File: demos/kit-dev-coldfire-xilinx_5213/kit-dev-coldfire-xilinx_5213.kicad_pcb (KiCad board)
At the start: 4 copper layers, 162 parts, among them J1 JACK_2P, P1 CONN_6, P3 CONN_2X2, P4 CONN_20X2, Q1 3906, SW1 SW_PUSH, SW2 SW_PUSH, U1 MCF5213-LQFP100, U2 74AHC1G14, U3 MAX202, U4 74HC125, U5 MAX202, U7 PCA82C251, U8 MAX202, U9 XCR3256-TQ144, Y1 8MHz

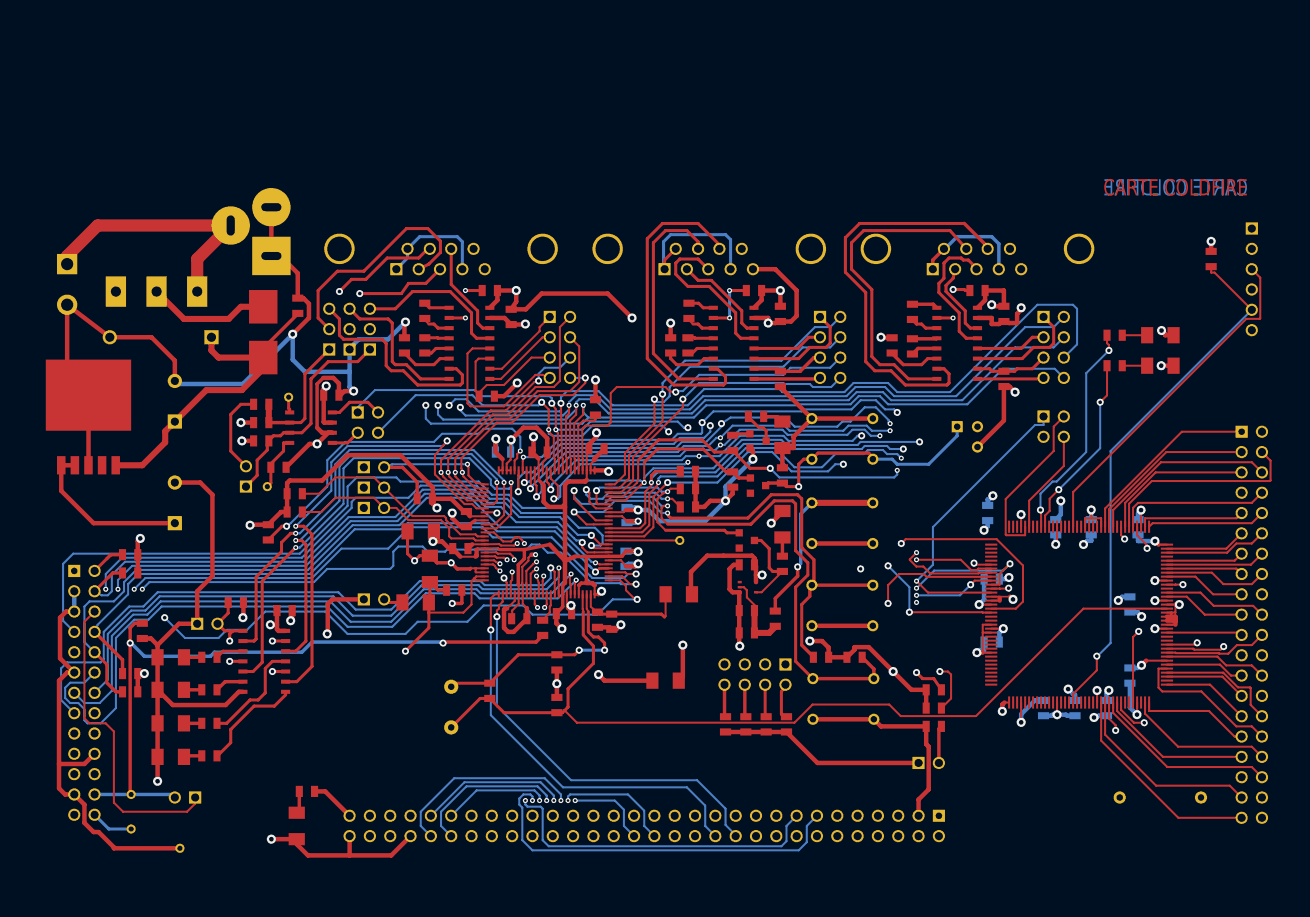
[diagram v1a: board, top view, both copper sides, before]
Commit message: Update demo files. A minor code cleaning.
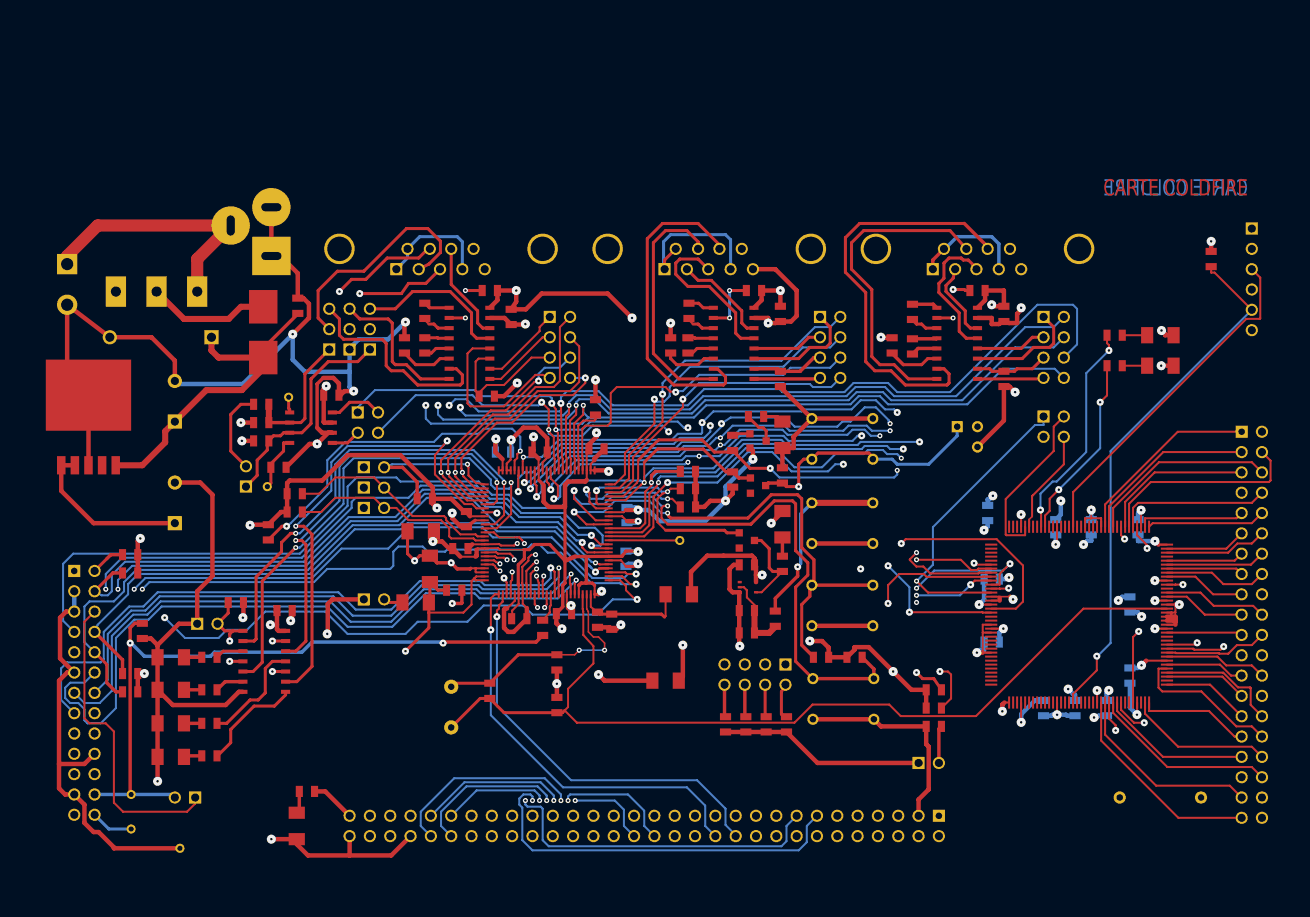
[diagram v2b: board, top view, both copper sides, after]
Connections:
- net +3.3V renamed VCC
- net /CANTX renamed /inout_user/CANTX
- net /DSPI_DOUT renamed /inout_user/QSPI_DOUT
- net /PWM1 renamed /inout_user/PWM1
- net /PWM3 renamed /inout_user/PWM3
- net /QSPI_DIN renamed /inout_user/QSPI_DIN
- net /RCON- renamed /inout_user/RCON-
- net /RSTI- renamed /inout_user/RSTI-
- net /RSTO- renamed /inout_user/RTS0-
- net /UCTS0 renamed /inout_user/UCTS0
- net /URTS1 renamed /inout_user/URTS1
- net /URXD0 renamed /inout_user/URXD0
- net /UTXD1 renamed /inout_user/UTXD1
- net /UTXD2 renamed /inout_user/UTXD2
- net /VCCA renamed /inout_user/VCCA
- net /inout_user/AN0 renamed /AN0
- net /inout_user/AN1 renamed /AN1
- net /inout_user/AN5 renamed /AN5
- net /inout_user/AN7 renamed /AN7
- net /inout_user/DTIN0 renamed /DTIN0
- net /inout_user/DTIN2 renamed /DTIN2
- net /inout_user/DTIN3 renamed /DTIN3
- net /inout_user/GPT0 renamed /GPT0
- net /inout_user/GPT2 renamed /GPT2
- net /inout_user/IRQ-4 renamed /IRQ-4
- net /inout_user/QSPI_CS0 renamed /QSPI_CS0
- net /inout_user/QSPI_CS1 renamed /xilinx/QSPI_CS1
- net /inout_user/VRL renamed GNDA
- net /xilinx/QSPI_SCLK renamed /inout_user/QSPI_SCLK
- net /xilinx/UCTS1- renamed /inout_user/UCTS1
- net /xilinx/XIL_INIT renamed /xilinx/IRQ-3
- net /xilinx/XIL_IRQ1 renamed /xilinx/IRQ-1
- net /xilinx/XIL_IRQ2 renamed /xilinx/IRQ-2
- P3 pad 4: N-000191 -> (no net)
- U9 pad 31: N-000191 -> (no net)
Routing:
- net N-000191: track 13.0 -> 0.00 mm
- net (no net): track 0.00 -> 13.0 mm
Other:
- net class Default: clearance 0.254 -> 0.16; trace_width 0.19812 -> 0.25; via_drill 0.635 -> 0.3
- net class power added: clearance 0.16, trace_width 0.4, via_dia 0.635, via_drill 0.3
- rule trace_clearance: 0.254 -> 0.16
- rule trace_min: 0.19812 -> 0.18
- rule via_min_drill: 0.508 -> 0.2
- rule via_min_size: 0.635 -> 0.45

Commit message: add patch from Cirilo Bernardo, and minor fixes.
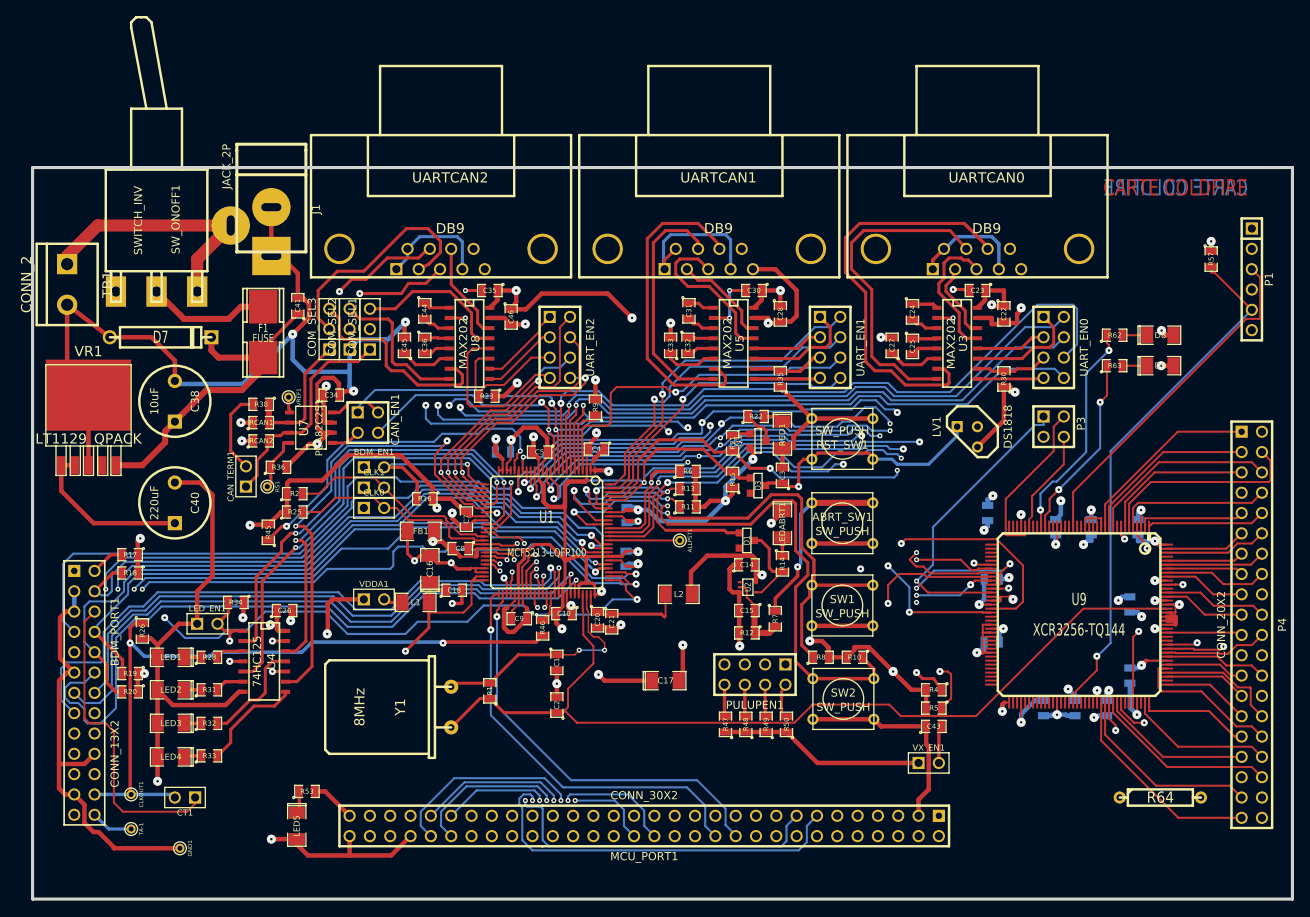
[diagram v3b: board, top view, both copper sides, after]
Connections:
- net VCC renamed VDD
- BDM_PORT1 pad 1: (no net) -> Net-(BDM_PORT1-Pad1)
- BDM_PORT1 pad 21: (no net) -> Net-(BDM_PORT1-Pad21)
- BDM_PORT1 pad 22: (no net) -> Net-(BDM_PORT1-Pad22)
- P3 pad 4: (no net) -> Net-(P3-Pad4)
- SW_ONOFF1 pad 1: (no net) -> Net-(SW_ONOFF1-Pad1)
- U9 pad 102: (no net) -> Net-(U9-Pad102)
- U9 pad 103: (no net) -> Net-(U9-Pad103)
- U9 pad 106: (no net) -> Net-(U9-Pad106)
- U9 pad 110: (no net) -> Net-(U9-Pad110)
- U9 pad 120: (no net) -> Net-(U9-Pad120)
- U9 pad 121: (no net) -> Net-(U9-Pad121)
- U9 pad 133: (no net) -> Net-(U9-Pad133)
- U9 pad 14: (no net) -> Net-(U9-Pad14)
- U9 pad 141: (no net) -> Net-(U9-Pad141)
- U9 pad 15: (no net) -> Net-(U9-Pad15)
- U9 pad 16: (no net) -> Net-(U9-Pad16)
- U9 pad 18: (no net) -> Net-(U9-Pad18)
- U9 pad 19: (no net) -> Net-(U9-Pad19)
- U9 pad 21: (no net) -> Net-(U9-Pad21)
- U9 pad 22: (no net) -> Net-(U9-Pad22)
- U9 pad 23: (no net) -> Net-(U9-Pad23)
- U9 pad 25: (no net) -> Net-(U9-Pad25)
- U9 pad 26: (no net) -> Net-(U9-Pad26)
- U9 pad 29: (no net) -> Net-(U9-Pad29)
- U9 pad 30: (no net) -> Net-(U9-Pad30)
- U9 pad 31: (no net) -> Net-(P3-Pad4)
- U9 pad 34: (no net) -> Net-(U9-Pad34)
- U9 pad 35: (no net) -> Net-(U9-Pad35)
- U9 pad 36: (no net) -> Net-(U9-Pad36)
- U9 pad 37: (no net) -> Net-(U9-Pad37)
- U9 pad 38: (no net) -> Net-(U9-Pad38)
- U9 pad 39: (no net) -> Net-(U9-Pad39)
- U9 pad 40: (no net) -> Net-(U9-Pad40)
- U9 pad 41: (no net) -> Net-(U9-Pad41)
- U9 pad 55: (no net) -> Net-(U9-Pad55)
- U9 pad 56: (no net) -> Net-(U9-Pad56)
- U9 pad 60: (no net) -> Net-(U9-Pad60)
- U9 pad 61: (no net) -> Net-(U9-Pad61)
- U9 pad 62: (no net) -> Net-(U9-Pad62)
- U9 pad 63: (no net) -> Net-(U9-Pad63)
- U9 pad 65: (no net) -> Net-(U9-Pad65)
- U9 pad 66: (no net) -> Net-(U9-Pad66)
- U9 pad 67: (no net) -> Net-(U9-Pad67)
- U9 pad 68: (no net) -> Net-(U9-Pad68)
- U9 pad 69: (no net) -> Net-(U9-Pad69)
- U9 pad 70: (no net) -> Net-(U9-Pad70)
- U9 pad 71: (no net) -> Net-(U9-Pad71)
- U9 pad 72: (no net) -> Net-(U9-Pad72)
- U9 pad 74: (no net) -> Net-(U9-Pad74)
- U9 pad 75: (no net) -> Net-(U9-Pad75)
- U9 pad 77: (no net) -> Net-(U9-Pad77)
- U9 pad 78: (no net) -> Net-(U9-Pad78)
- U9 pad 79: (no net) -> Net-(U9-Pad79)
- U9 pad 80: (no net) -> Net-(U9-Pad80)
- U9 pad 81: (no net) -> Net-(U9-Pad81)
- U9 pad 82: (no net) -> Net-(U9-Pad82)
- U9 pad 83: (no net) -> Net-(U9-Pad83)
- U9 pad 84: (no net) -> Net-(U9-Pad84)
- U9 pad 86: (no net) -> Net-(U9-Pad86)
- U9 pad 87: (no net) -> Net-(U9-Pad87)
- U9 pad 88: (no net) -> Net-(U9-Pad88)
- U9 pad 9: (no net) -> Net-(U9-Pad9)
- U9 pad 90: (no net) -> Net-(U9-Pad90)
- U9 pad 91: (no net) -> Net-(U9-Pad91)
- U9 pad 92: (no net) -> Net-(U9-Pad92)
- U9 pad 93: (no net) -> Net-(U9-Pad93)
- U9 pad 94: (no net) -> Net-(U9-Pad94)
- UARTCAN0 pad 9: (no net) -> Net-(UARTCAN0-Pad9)
- UARTCAN1 pad 9: (no net) -> Net-(UARTCAN1-Pad9)
- UARTCAN2 pad 9: (no net) -> Net-(UARTCAN2-Pad9)
- VR1 pad 4: (no net) -> Net-(VR1-Pad4)
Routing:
- net Net-(P3-Pad4): track 0.00 -> 13.0 mm
- net (no net): track 13.0 -> 0.00 mm
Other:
- board outline added: 157.5 x 91.4 mm
